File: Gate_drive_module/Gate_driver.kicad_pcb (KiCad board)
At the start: 2 copper layers, 0 parts

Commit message: Started work on PCB layout
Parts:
- added C1: 10u, Capacitors_SMD:C_0805_HandSoldering, F.Cu at (226.9, 116.2)
- added C10: 100n, Capacitors_SMD:C_0805_HandSoldering, F.Cu at (199.2, 145.1)
- added C11: 100n, Capacitors_SMD:C_0805_HandSoldering, F.Cu at (204.1, 146.5)
- added C2: 100n, Capacitors_SMD:C_0805_HandSoldering, F.Cu at (212.3, 139.4)
- added C3: 100u, Capacitors_SMD:C_1812_HandSoldering, F.Cu at (115.2, 131.7)
- added C4: 100u, Capacitors_SMD:C_1812_HandSoldering, F.Cu at (117.5, 122.3)
- added C5: 100u, Capacitors_SMD:C_1812_HandSoldering, F.Cu at (167.3, 140.6)
- added C6: 100p, Capacitors_SMD:C_0805_HandSoldering, F.Cu at (204.1, 141.0)
- added C7: 10u, Capacitors_SMD:C_0805_HandSoldering, F.Cu at (226.9, 121.8)
- added C8: 10u, Capacitors_SMD:C_0805_HandSoldering, F.Cu at (221.7, 126.3)
- added C9: 10u, Capacitors_SMD:C_0805_HandSoldering, F.Cu at (212.3, 133.8)
- added D1: RED PWR LED, LEDs:LED_0805_HandSoldering, F.Cu at (169.5, 131.7)
- added D2: D, Diodes_SMD:D_SMA_Handsoldering, F.Cu at (183.0, 144.3)
- added D3: D, Diodes_SMD:D_SMA_Handsoldering, F.Cu at (193.1, 138.7)
- added D4: ES1F, Diodes_SMD:D_SMA_Handsoldering, F.Cu at (199.5, 127.9)
- added D5: GREEN PWR LED, LEDs:LED_0805_HandSoldering, F.Cu at (183.1, 126.2)
- added D6: GREEN PWR LED, LEDs:LED_0805_HandSoldering, F.Cu at (170.4, 126.2)
- added J1: CONN_01X10, Pin_Headers:Pin_Header_Straight_1x10_Pitch2.54mm, F.Cu at (103.3, 140.6)
- added J2: CONN_01X04, PhoenixContact:MSTBA_25_4p_G_508-1757268, F.Cu at (125.0, 160.1)
- added J3: CONN_01X03, PhoenixContact:MSTBA_25_3p_G_508-1757488, F.Cu at (191.8, 111.0)
- added J4: CONN_01X03, Pin_Headers:Pin_Header_Straight_1x03_Pitch2.54mm, F.Cu at (179.6, 103.9)
- added J5: CONN_01X03, PhoenixContact:MSTBA_25_3p_G_508-1757488, F.Cu at (210.2, 111.0)
- added R1: 10k, Resistors_SMD:R_0805_HandSoldering, F.Cu at (209.2, 144.9)
- added R2: 10k, Resistors_SMD:R_0805_HandSoldering, F.Cu at (227.6, 132.8)
- added R3: 10k, Resistors_SMD:R_0805_HandSoldering, F.Cu at (121.7, 116.8)
- added R4: 100R, Resistors_SMD:R_0805_HandSoldering, F.Cu at (219.5, 144.8)
- added R5: 100R, Resistors_SMD:R_0805_HandSoldering, F.Cu at (217.3, 133.8)
- added R6: 100R, Resistors_SMD:R_0805_HandSoldering, F.Cu at (222.5, 138.3)
- added R7: 100k, Resistors_SMD:R_0805_HandSoldering, F.Cu at (214.3, 144.9)
- added R8: 10k, Resistors_SMD:R_0805_HandSoldering, F.Cu at (217.3, 139.3)
- added R9: 10k, Resistors_SMD:R_0805_HandSoldering, F.Cu at (222.5, 132.8)
- added TP1: TEST, Pin_Headers:Pin_Header_Straight_1x01_Pitch2.54mm, F.Cu at (226.5, 110.1)
- added U1: HCPL-316J, SMD_Packages:SO-16-W, F.Cu at (135.4, 120.8)
- added U2: Mornsun_QA01C, Mornsun:QA01C, F.Cu at (135.0, 134.1)

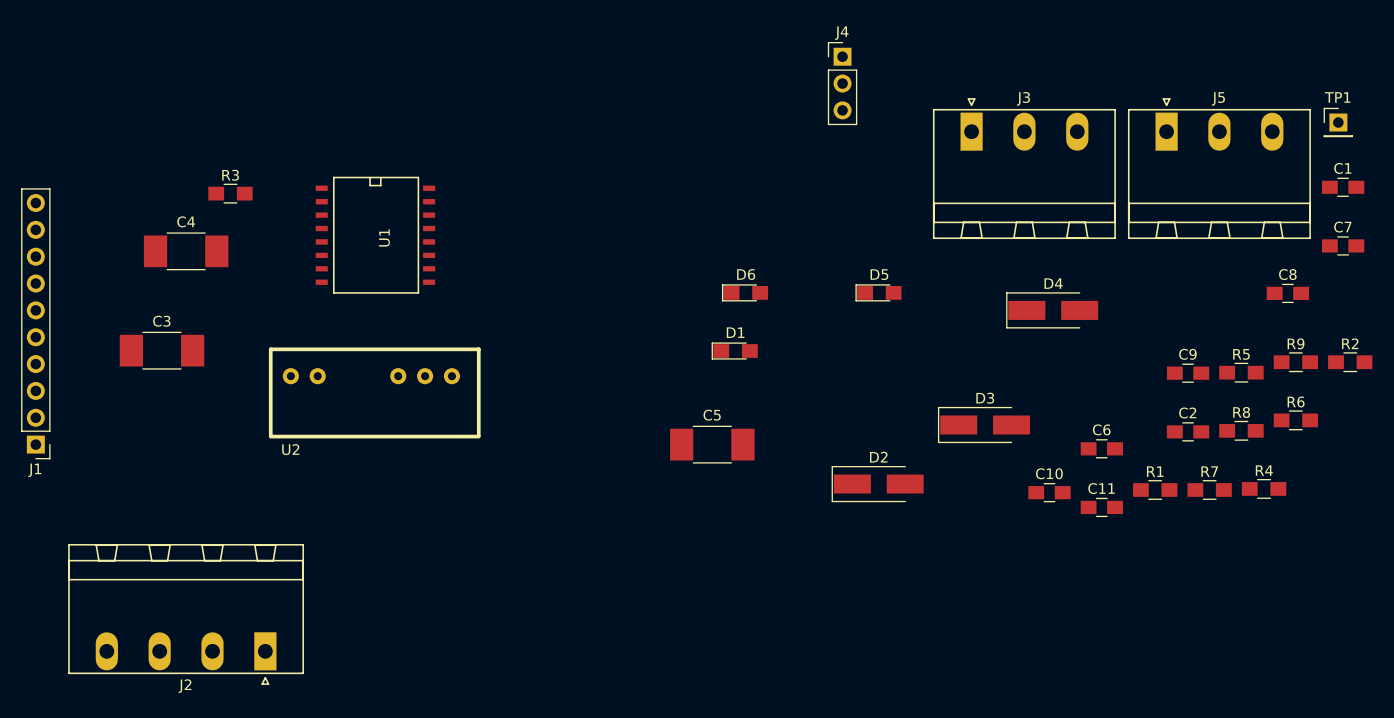
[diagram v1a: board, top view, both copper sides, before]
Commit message: Updated component value
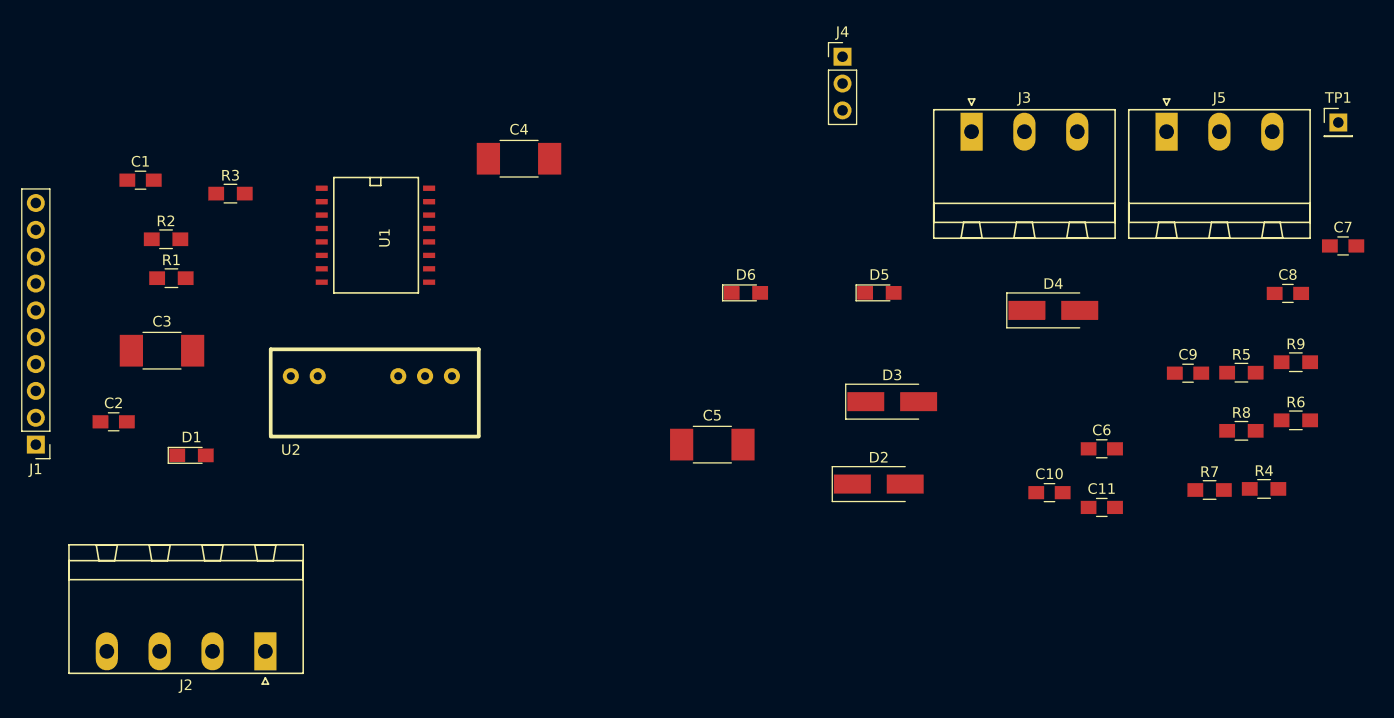
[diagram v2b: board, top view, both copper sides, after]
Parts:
- moved C1 113.8 mm to (113.2, 115.6)
- moved R2 112.6 mm to (115.6, 121.2)
- moved C2 101.7 mm to (110.6, 138.4)
- moved R1 95.2 mm to (116.1, 124.8)
- moved D1 52.4 mm to (118.0, 141.6)
- moved C4 32.7 mm to (149.0, 113.5)
- moved D3 9.06 mm to (184.3, 136.5)
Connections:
- C10 pad 1: VCC -> VCC_ISO
- C10 pad 2: GND -> GND_ISO
- C11 pad 1: GND -> GND_ISO
- C11 pad 2: VCC -> VEE_ISO
- C4 pad 1: VCC -> VCC_ISO
- C4 pad 2: GND -> GND_ISO
- C5 pad 1: GND -> GND_ISO
- C5 pad 2: VCC -> VEE_ISO
- C6 pad 2: GND -> GND_ISO
- C7 pad 1: VCC -> VCC_ISO
- C7 pad 2: VCC -> VEE_ISO
- C8 pad 1: VCC -> VCC_ISO
- C8 pad 2: GND -> GND_ISO
- C9 pad 1: GND -> GND_ISO
- C9 pad 2: VCC -> VEE_ISO
- D5 pad 1: GND -> GND_ISO
- D6 pad 1: VCC -> VEE_ISO
- J3 pad 1: VCC -> VEE_ISO
- J3 pad 2: GND -> GND_ISO
- J3 pad 3: VCC -> VCC_ISO
- J4 pad 3: GND -> GND_ISO
- J5 pad 3: GND -> GND_ISO
- R7 pad 1: GND -> GND_ISO
- R8 pad 1: VCC -> VCC_ISO
- R9 pad 1: GND -> GND_ISO
- U1 pad 10: VCC -> VEE_ISO
- U1 pad 12: VCC -> VCC_ISO
- U1 pad 13: VCC -> VCC_ISO
- U1 pad 16: GND -> GND_ISO
- U1 pad 9: VCC -> VEE_ISO
- U2 pad 5: VCC -> VEE_ISO
- U2 pad 6: GND -> GND_ISO
- U2 pad 7: VCC -> VCC_ISO
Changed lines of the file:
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@@
 (kicad_pcb (version 4) (host pcbnew 4.0.6)
   (general
-    (links 74)
-    (no_connects 74)
-    (area 96.439667 100.581 230.191002 164.422)
+    (links 71)
+    (no_connects 71)
+    (area 0 0 0 0)
     (thickness 1.6)
     (drawings 0)
@@
     (zones 0)
     (modules 34)
-    (nets 24)
+    (nets 27)
   )
   (page A4)
@@
   (net 22 "Net-(U1-Pad7)")
   (net 23 "Net-(U1-Pad15)")
+  (net 24 VCC_ISO)
+  (net 25 GND_ISO)
+  (net 26 VEE_ISO)
   (net_class Default "This is the default net class."
     (clearance 0.2)
@@
     (add_net +15V)
     (add_net GND)
+    (add_net GND_ISO)
     (add_net "Net-(C6-Pad1)")
     (add_net "Net-(D1-Pad2)")
@@
     (add_net "Net-(U1-Pad7)")
     (add_net VCC)
+    (add_net VCC_ISO)
+    (add_net VEE_ISO)
   )
   (module Capacitors_SMD:C_0805_HandSoldering (layer F.Cu)
-    (at 226.936001 116.242)
+    (at 113.157 115.57)
     (descr "Capacitor SMD 0805, hand soldering")
     (tags "capacitor 0805")
@@
   )
   (module Capacitors_SMD:C_0805_HandSoldering (layer F.Cu)
-    (at 212.266001 139.382)
+    (at 110.617 138.43)
     (descr "Capacitor SMD 0805, hand soldering")
     (tags "capacitor 0805")
@@
   )
   (module Capacitors_SMD:C_1812_HandSoldering (layer F.Cu)
-    (at 117.475 122.301)
+    (at 148.971 113.538)
     (descr "Capacitor SMD 1812, hand soldering")
     (tags "capacitor 1812")
@@
     (fp_line (start 4.25 1.85) (end -4.25 1.85) (layer F.CrtYd) (width 0.05))
     (pad 1 smd rect (at -2.9 0) (size 2.2 3) (layers F.Cu F.Paste F.Mask)
-      (net 1 VCC))
+      (net 24 VCC_ISO))
     (pad 2 smd rect (at 2.9 0) (size 2.2 3) (layers F.Cu F.Paste F.Mask)
-      (net 2 GND))
+      (net 25 GND_ISO))
     (model Capacitors_SMD.3dshapes/C_1812.wrl
       (at (xyz 0 0 0))
@@
     (fp_line (start 4.25 1.85) (end -4.25 1.85) (layer F.CrtYd) (width 0.05))
     (pad 1 smd rect (at -2.9 0) (size 2.2 3) (layers F.Cu F.Paste F.Mask)
-      (net 2 GND))
+      (net 25 GND_ISO))
     (pad 2 smd rect (at 2.9 0) (size 2.2 3) (layers F.Cu F.Paste F.Mask)
-      (net 1 VCC))
+      (net 26 VEE_ISO))
     (model Capacitors_SMD.3dshapes/C_1812.wrl
       (at (xyz 0 0 0))
@@
       (net 4 "Net-(C6-Pad1)"))
     (pad 2 smd rect (at 1.25 0) (size 1.5 1.25) (layers F.Cu F.Paste F.Mask)
-      (net 2 GND))
+      (net 25 GND_ISO))
     (model Capacitors_SMD.3dshapes/C_0805.wrl
       (at (xyz 0 0 0))
@@
     (fp_line (start 2.25 0.87) (end -2.25 0.87) (layer F.CrtYd) (width 0.05))
     (pad 1 smd rect (at -1.25 0) (size 1.5 1.25) (layers F.Cu F.Paste F.Mask)
-      (net 1 VCC))
+      (net 24 VCC_ISO))
     (pad 2 smd rect (at 1.25 0) (size 1.5 1.25) (layers F.Cu F.Paste F.Mask)
-      (net 1 VCC))
+      (net 26 VEE_ISO))
     (model Capacitors_SMD.3dshapes/C_0805.wrl
       (at (xyz 0 0 0))
@@
     (fp_line (start 2.25 0.87) (end -2.25 0.87) (layer F.CrtYd) (width 0.05))
     (pad 1 smd rect (at -1.25 0) (size 1.5 1.25) (layers F.Cu F.Paste F.Mask)
-      (net 1 VCC))
+      (net 24 VCC_ISO))
     (pad 2 smd rect (at 1.25 0) (size 1.5 1.25) (layers F.Cu F.Paste F.Mask)
-      (net 2 GND))
+      (net 25 GND_ISO))
     (model Capacitors_SMD.3dshapes/C_0805.wrl
       (at (xyz 0 0 0))
@@
     (fp_line (start 2.25 0.87) (end -2.25 0.87) (layer F.CrtYd) (width 0.05))
     (pad 1 smd rect (at -1.25 0) (size 1.5 1.25) (layers F.Cu F.Paste F.Mask)
-      (net 2 GND))
+      (net 25 GND_ISO))
     (pad 2 smd rect (at 1.25 0) (size 1.5 1.25) (layers F.Cu F.Paste F.Mask)
-      (net 1 VCC))
+      (net 26 VEE_ISO))
     (model Capacitors_SMD.3dshapes/C_0805.wrl
       (at (xyz 0 0 0))
@@
     (fp_line (start 2.25 0.87) (end -2.25 0.87) (layer F.CrtYd) (width 0.05))
     (pad 1 smd rect (at -1.25 0) (size 1.5 1.25) (layers F.Cu F.Paste F.Mask)
-      (net 1 VCC))
+      (net 24 VCC_ISO))
     (pad 2 smd rect (at 1.25 0) (size 1.5 1.25) (layers F.Cu F.Paste F.Mask)
-      (net 2 GND))
+      (net 25 GND_ISO))
     (model Capacitors_SMD.3dshapes/C_0805.wrl
       (at (xyz 0 0 0))
@@
     (fp_line (start 2.25 0.87) (end -2.25 0.87) (layer F.CrtYd) (width 0.05))
     (pad 1 smd rect (at -1.25 0) (size 1.5 1.25) (layers F.Cu F.Paste F.Mask)
-      (net 2 GND))
+      (net 25 GND_ISO))
     (pad 2 smd rect (at 1.25 0) (size 1.5 1.25) (layers F.Cu F.Paste F.Mask)
-      (net 1 VCC))
+      (net 26 VEE_ISO))
     (model Capacitors_SMD.3dshapes/C_0805.wrl
       (at (xyz 0 0 0))
@@
   )
   (module LEDs:LED_0805_HandSoldering (layer F.Cu)
-    (at 169.453857 131.732)
+    (at 117.983 141.605)
     (descr "Resistor SMD 0805, hand soldering")
     (tags "resistor 0805")
@@
   )
   (module Diodes_SMD:D_SMA_Handsoldering (layer F.Cu)
-    (at 193.066001 138.732)
+    (at 184.277 136.525)
     (descr "Diode SMA (DO-214AC) Handsoldering")
     (tags "Diode SMA (DO-214AC) Handsoldering")
@@
     (fp_line (start -2.2 -0.75) (end -2.2 0.75) (layer F.SilkS) (width 0.12))
     (pad 1 smd rect (at -1.35 0) (size 1.5 1.3) (layers F.Cu F.Paste F.Mask)
-      (net 2 GND))
+      (net 25 GND_ISO))
     (pad 2 smd rect (at 1.35 0) (size 1.5 1.3) (layers F.Cu F.Paste F.Mask)
       (net 11 "Net-(D5-Pad2)"))
@@
     (fp_line (start -2.2 -0.75) (end -2.2 0.75) (layer F.SilkS) (width 0.12))
     (pad 1 smd rect (at -1.35 0) (size 1.5 1.3) (layers F.Cu F.Paste F.Mask)
-      (net 1 VCC))
+      (net 26 VEE_ISO))
     (pad 2 smd rect (at 1.35 0) (size 1.5 1.3) (layers F.Cu F.Paste F.Mask)
       (net 12 "Net-(D6-Pad2)"))
@@
     (fp_line (start -0.3 -3.1) (end 0 -2.5) (layer F.SilkS) (width 0.15))
     (pad 1 thru_hole rect (at 0 0) (size 2.1 3.6) (drill 1.4) (layers *.Cu *.Mask)
-      (net 1 VCC))
+      (net 26 VEE_ISO))
     (pad 2 thru_hole oval (at 5 0) (size 2.1 3.6) (drill 1.4) (layers *.Cu *.Mask)
-      (net 2 GND))
+      (net 25 GND_ISO))
     (pad 3 thru_hole oval (at 10 0) (size 2.1 3.6) (drill 1.4) (layers *.Cu *.Mask)
-      (net 1 VCC))
+      (net 24 VCC_ISO))
     (model /Users/Yngve/git/Switchcraft/kicad-lib/packages3d/PhoenixContact.3dshapes/MSTBA_25_3p_G_508-1757488.wrl
       (at (xyz 0 0 0))
@@
       (net 21 "Net-(J4-Pad2)"))
     (pad 3 thru_hole oval (at 0 5.08) (size 1.7 1.7) (drill 1) (layers *.Cu *.Mask)
-      (net 2 GND))
+      (net 25 GND_ISO))
     (model ${KISYS3DMOD}/Pin_Headers.3dshapes/Pin_Header_Straight_1x03_Pitch2.54mm.wrl
       (at (xyz 0 0 0))
@@
       (net 21 "Net-(J4-Pad2)"))
     (pad 3 thru_hole oval (at 10 0) (size 2.1 3.6) (drill 1.4) (layers *.Cu *.Mask)
-      (net 2 GND))
+      (net 25 GND_ISO))
     (model /Users/Yngve/git/Switchcraft/kicad-lib/packages3d/PhoenixContact.3dshapes/MSTBA_25_3p_G_508-1757488.wrl
       (at (xyz 0 0 0))
@@
   )
   (module Resistors_SMD:R_0805_HandSoldering (layer F.Cu)
-    (at 209.156001 144.882)
+    (at 116.078 124.841)
     (descr "Resistor SMD 0805, hand soldering")
     (tags "resistor 0805")
@@
   )
   (module Resistors_SMD:R_0805_HandSoldering (layer F.Cu)
-    (at 227.616001 132.792)
+    (at 115.57 121.158)
     (descr "Resistor SMD 0805, hand soldering")
     (tags "resistor 0805")
@@
     (fp_line (start 2.35 0.9) (end -2.35 0.9) (layer F.CrtYd) (width 0.05))
     (pad 1 smd rect (at -1.35 0) (size 1.5 1.3) (layers F.Cu F.Paste F.Mask)
-      (net 2 GND))
+      (net 25 GND_ISO))
     (pad 2 smd rect (at 1.35 0) (size 1.5 1.3) (layers F.Cu F.Paste F.Mask)
       (net 21 "Net-(J4-Pad2)"))
@@
     (fp_line (start 2.35 0.9) (end -2.35 0.9) (layer F.CrtYd) (width 0.05))
     (pad 1 smd rect (at -1.35 0) (size 1.5 1.3) (layers F.Cu F.Paste F.Mask)
-      (net 1 VCC))
+      (net 24 VCC_ISO))
     (pad 2 smd rect (at 1.35 0) (size 1.5 1.3) (layers F.Cu F.Paste F.Mask)
       (net 11 "Net-(D5-Pad2)"))
@@
     (fp_line (start 2.35 0.9) (end -2.35 0.9) (layer F.CrtYd) (width 0.05))
     (pad 1 smd rect (at -1.35 0) (size 1.5 1.3) (layers F.Cu F.Paste F.Mask)
-      (net 2 GND))
+      (net 25 GND_ISO))
     (pad 2 smd rect (at 1.35 0) (size 1.5 1.3) (layers F.Cu F.Paste F.Mask)
       (net 12 "Net-(D6-Pad2)"))
@@
       (net 2 GND))
     (pad 9 smd rect (at 4.445 -5.08 270) (size 0.508 1.143) (layers F.Cu F.Paste F.Mask)
-      (net 1 VCC))
+      (net 26 VEE_ISO))
     (pad 10 smd rect (at 3.175 -5.08 270) (size 0.508 1.143) (layers F.Cu F.Paste F.Mask)
-      (net 1 VCC))
+      (net 26 VEE_ISO))
     (pad 11 smd rect (at 1.905 -5.08 270) (size 0.508 1.143) (layers F.Cu F.Paste F.Mask)
       (net 7 "Net-(D2-Pad2)"))
     (pad 12 smd rect (at 0.635 -5.08 270) (size 0.508 1.143) (layers F.Cu F.Paste F.Mask)
-      (net 1 VCC))
+      (net 24 VCC_ISO))
     (pad 13 smd rect (at -0.635 -5.08 270) (size 0.508 1.143) (layers F.Cu F.Paste F.Mask)
-      (net 1 VCC))
+      (net 24 VCC_ISO))
     (pad 14 smd rect (at -1.905 -5.08 270) (size 0.508 1.143) (layers F.Cu F.Paste F.Mask)
       (net 4 "Net-(C6-Pad1)"))
@@
       (net 23 "Net-(U1-Pad15)"))
     (pad 16 smd rect (at -4.445 -5.08 270) (size 0.508 1.143) (layers F.Cu F.Paste F.Mask)
-      (net 2 GND))
+      (net 25 GND_ISO))
     (model SMD_Packages.3dshapes/SO-16-W.wrl
       (at (xyz 0 0 0))
@@
       (net 2 GND))
     (pad 5 thru_hole circle (at 2.54 0) (size 1.524 1.524) (drill 0.762) (layers *.Cu *.Mask)
-      (net 1 VCC))
+      (net 26 VEE_ISO))
     (pad 6 thru_hole circle (at 5.08 0) (size 1.524 1.524) (drill 0.762) (layers *.Cu *.Mask)
-      (net 2 GND))
+      (net 25 GND_ISO))
     (pad 7 thru_hole circle (at 7.62 0) (size 1.524 1.524) (drill 0.762) (layers *.Cu *.Mask)
-      (net 1 VCC))
+      (net 24 VCC_ISO))
   )
 )

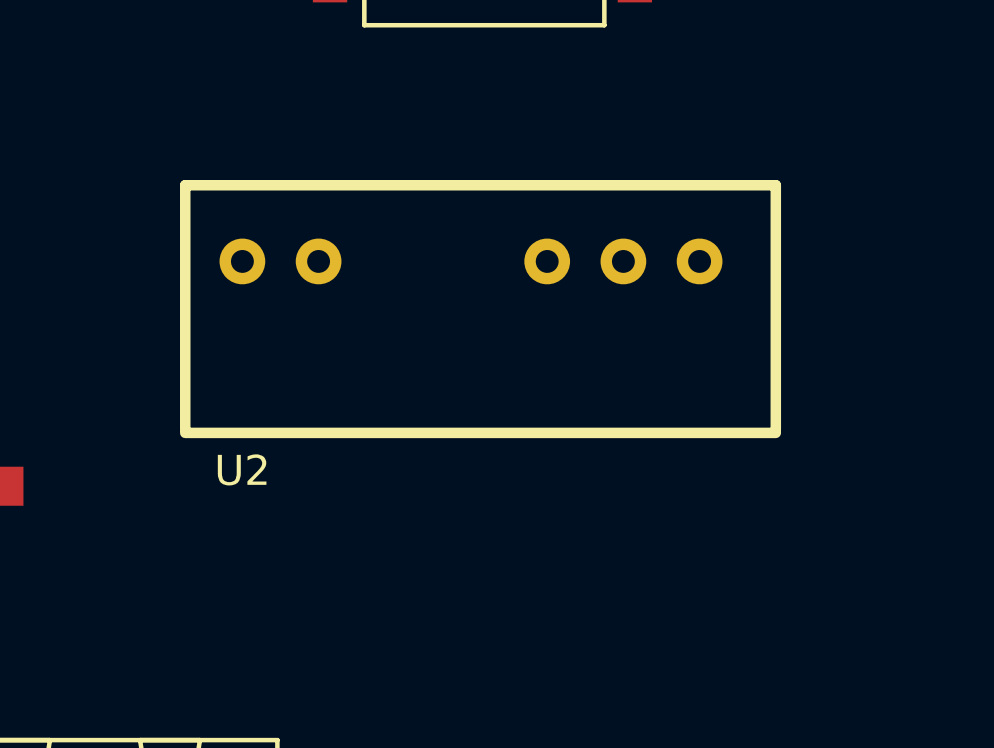
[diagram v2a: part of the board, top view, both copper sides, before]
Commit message: Updated footprint for mornsun with 3D model and correct courtyard
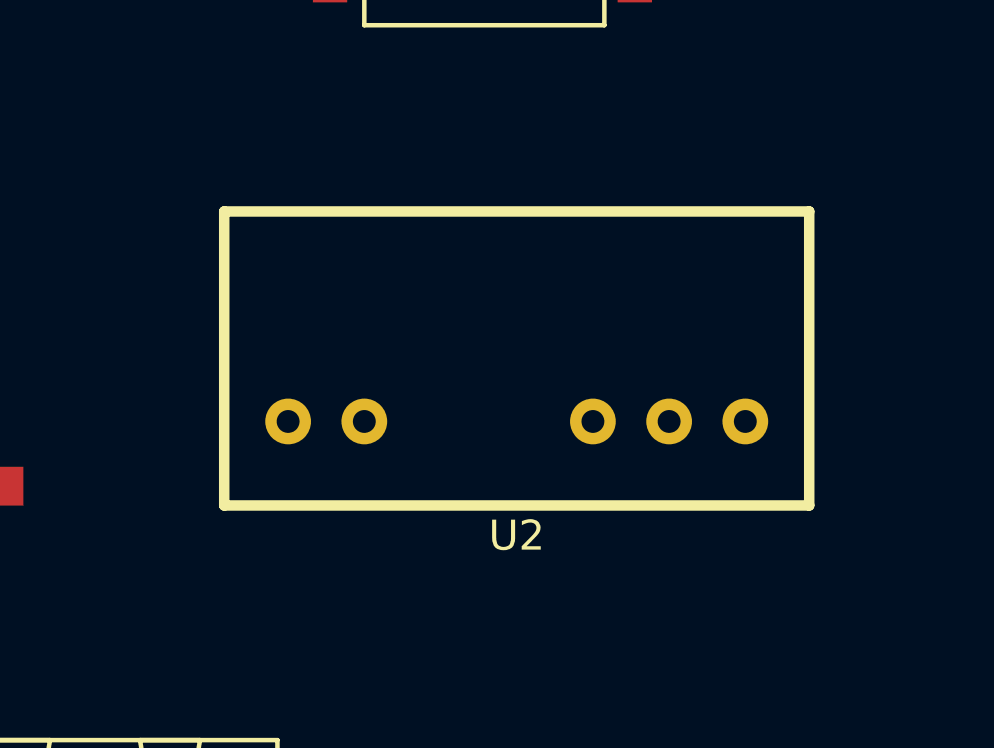
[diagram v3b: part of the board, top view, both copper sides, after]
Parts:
- U2: footprint Mornsun:QA01C -> mornsun:QA01C
- moved U2 5.55 mm to (136.5, 139.4)
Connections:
- J1 pad 2: Net-(J1-Pad2) -> (no net)
- J1 pad 3: Net-(J1-Pad3) -> (no net)
- J1 pad 9: Net-(J1-Pad9) -> (no net)
- J2 pad 3: Net-(J2-Pad3) -> (no net)
- U1 pad 15: Net-(U1-Pad15) -> (no net)
- U1 pad 7: Net-(U1-Pad7) -> (no net)
